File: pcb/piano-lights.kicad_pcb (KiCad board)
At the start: 2 copper layers, 150 x 82 mm, 30 parts, among them J1 FTDI RS232, J2 USB_B_Micro, J3 LED Strip, J4 AVR-ISP-6, J5 MIDI IN, J6 MIDI THRU, SW1 Button, SW2 Reset, U1 ATmega328P-P, U2 H11L1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

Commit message: PCB tweaks
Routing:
- net /DEBUG_TX: track 60.7 -> 61.8 mm
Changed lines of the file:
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@@
     (property "Sheetname" "")
     (attr smd)
-    (fp_text reference "R1" (at 0 -1.65 90) (layer "F.SilkS")
-      (effects (font (size 1 1) (thickness 0.15)))
-    )
-    (fp_text value "2k2" (at 0 1.65 90) (layer "F.Fab")
+    (fp_text reference "R1" (at 2.5 0 180) (layer "F.SilkS")
+      (effects (font (size 1 1) (thickness 0.15)))
+    )
+    (fp_text value "2k2" (at -2.75 0 180) (layer "F.Fab")
       (effects (font (size 1 1) (thickness 0.15)))
     )
@@
     (property "Sheetname" "")
     (attr through_hole)
-    (fp_text reference "C4" (at 1 -3.75 90) (layer "F.SilkS")
-      (effects (font (size 1 1) (thickness 0.15)))
-    )
-    (fp_text value "10u" (at 1 3.75 90) (layer "F.Fab")
+    (fp_text reference "C4" (at -2.75 0 180) (layer "F.SilkS")
+      (effects (font (size 1 1) (thickness 0.15)))
+    )
+    (fp_text value "10u" (at 4.5 0 180) (layer "F.Fab")
       (effects (font (size 1 1) (thickness 0.15)))
     )
@@
     (property "Sheetname" "")
     (attr smd)
-    (fp_text reference "U3" (at 0 -2.9 90) (layer "F.SilkS")
-      (effects (font (size 1 1) (thickness 0.15)))
-    )
-    (fp_text value "74AHC1G125" (at 0 2.9 90) (layer "F.Fab")
+    (fp_text reference "U3" (at 0 -2.9 180) (layer "F.SilkS")
+      (effects (font (size 1 1) (thickness 0.15)))
+    )
+    (fp_text value "74AHC1G125" (at -0.061 6.758 180) (layer "F.Fab")
       (effects (font (size 1 1) (thickness 0.15)))
     )
@@
   (via (at 118.618 97.536) (size 0.762) (drill 0.381) (layers "F.Cu" "B.Cu") (net 4))
   (segment (start 137.17 90.287) (end 137.17 87.112) (width 0.508) (layer "B.Cu") (net 4))
-  (segment (start 176.5 84.044) (end 176.5 78.8) (width 0.508) (layer "B.Cu") (net 4))
+  (segment (start 176.525 88.407) (end 176.525 78.825) (width 0.508) (layer "B.Cu") (net 4))
   (segment (start 119.507 97.536) (end 120.904 98.933) (width 0.508) (layer "B.Cu") (net 4))
   (segment (start 118.618 97.536) (end 119.507 97.536) (width 0.508) (layer "B.Cu") (net 4))
-  (segment (start 176.525 84.069) (end 176.5 84.044) (width 0.508) (layer "B.Cu") (net 4))
   (segment (start 134.63 94.732) (end 134.63 92.827) (width 0.508) (layer "B.Cu") (net 4))
   (segment (start 134.63 92.827) (end 137.17 90.287) (width 0.508) (layer "B.Cu") (net 4))
-  (segment (start 176.525 88.407) (end 176.525 84.069) (width 0.508) (layer "B.Cu") (net 4))
+  (segment (start 176.525 78.825) (end 176.5 78.8) (width 0.508) (layer "B.Cu") (net 4))
   (segment (start 111.52 110.48) (end 110 112) (width 0.254) (layer "F.Cu") (net 5))
   (segment (start 110 112) (end 101.84 112) (width 0.254) (layer "F.Cu") (net 5))
@@
   (segment (start 168.656 108.712) (end 186.944 108.712) (width 0.254) (layer "F.Cu") (net 24))
   (segment (start 153.15 84.8) (end 179.05 84.8) (width 0.254) (layer "F.Cu") (net 25))
-  (segment (start 183.85 84.85) (end 188.3 84.85) (width 0.254) (layer "F.Cu") (net 25))
   (segment (start 179.05 84.8) (end 179.15 84.9) (width 0.254) (layer "F.Cu") (net 25))
   (segment (start 152.41 85.54) (end 153.15 84.8) (width 0.254) (layer "F.Cu") (net 25))
+  (segment (start 189.45 86) (end 189.45 105.55) (width 0.254) (layer "F.Cu") (net 25))
+  (segment (start 183.85 84.85) (end 188.3 84.85) (width 0.254) (layer "F.Cu") (net 25))
   (segment (start 188.3 84.85) (end 189.45 86) (width 0.254) (layer "F.Cu") (net 25))
-  (segment (start 189.45 86) (end 189.45 103.666) (width 0.254) (layer "F.Cu") (net 25))
   (segment (start 152.41 87.112) (end 152.41 85.54) (width 0.254) (layer "F.Cu") (net 25))
-  (segment (start 189.45 103.666) (end 186.944 106.172) (width 0.254) (layer "F.Cu") (net 25))
+  (segment (start 189.45 105.55) (end 188.828 106.172) (width 0.254) (layer "F.Cu") (net 25))
+  (segment (start 188.828 106.172) (end 186.944 106.172) (width 0.254) (layer "F.Cu") (net 25))
   (via (at 183.85 84.85) (size 0.762) (drill 0.381) (layers "F.Cu" "B.Cu") (net 25))
   (via (at 179.15 84.9) (size 0.762) (drill 0.381) (layers "F.Cu" "B.Cu") (net 25))
@@
         (xy 188.1 59)
         (xy 188.08 55)
-        (xy 189.131428 54.999387)
+        (xy 188.53 55)
+        (xy 189.13172 55.499387)
       )
     )

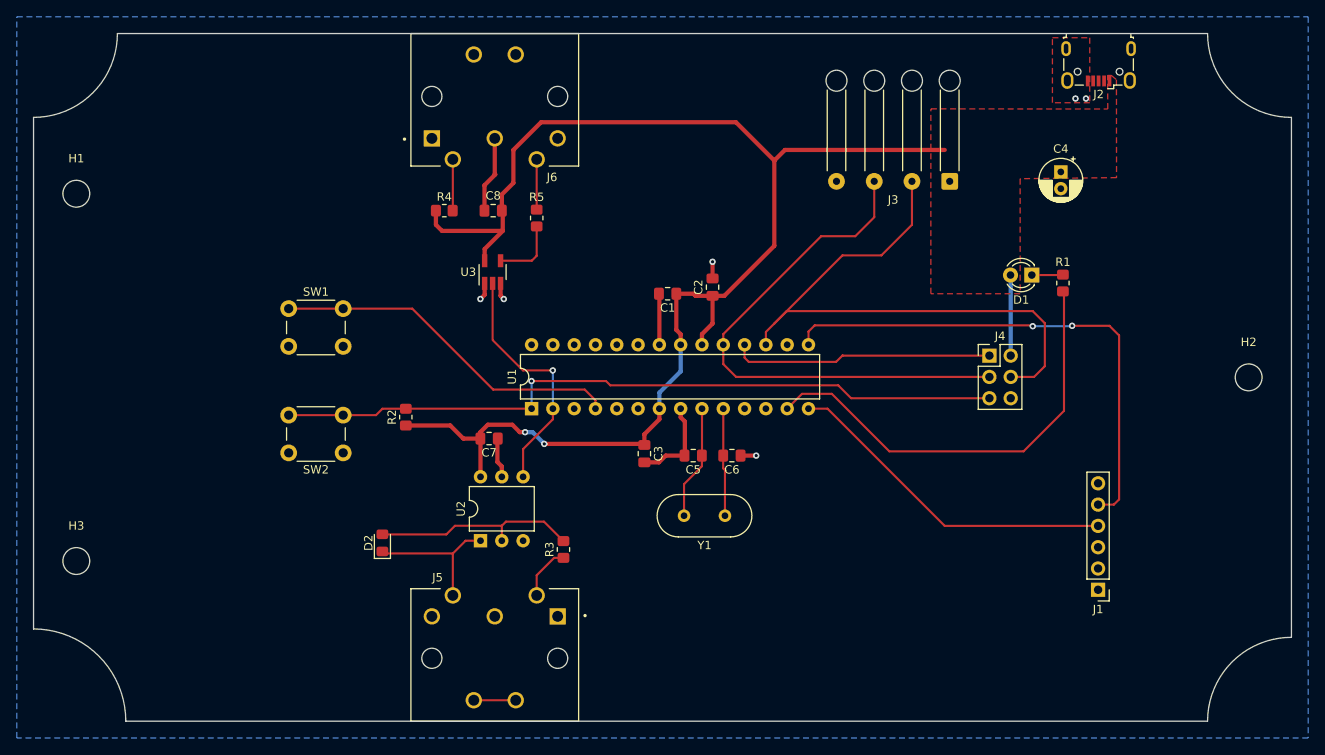
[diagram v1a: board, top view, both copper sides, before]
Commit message: Fix up silk screen. Fix all DRC errors. Tweak position of LED holes.
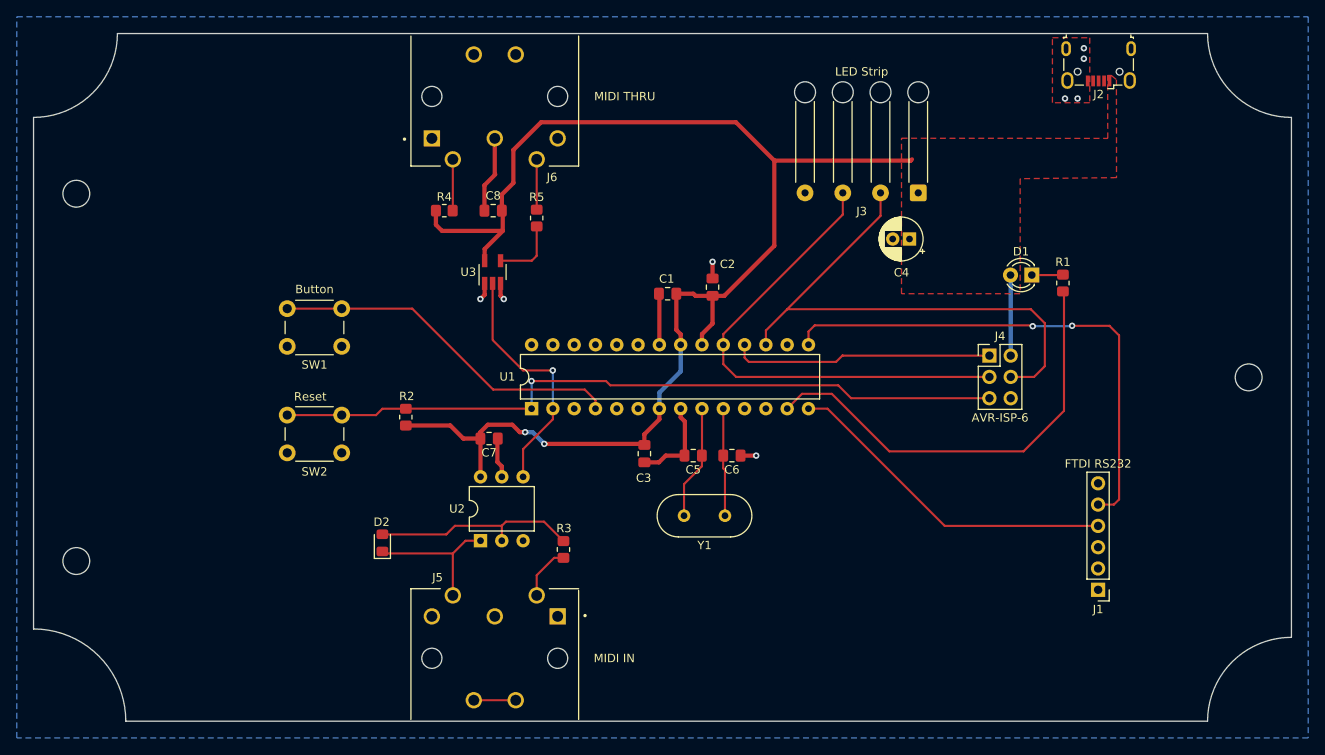
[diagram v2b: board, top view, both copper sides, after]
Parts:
- moved C4 19.7 mm to (164.5, 74.5), turned to 180 degrees
- moved J3 3.99 mm to (165.5, 69.0)
- moved SW2 0.17 mm to (96.8, 100.0)
- moved SW1 0.17 mm to (90.2, 82.8)
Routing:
- net /PICO: track 72.6 -> 64.9 mm
- net /SCK: track 64.0 -> 58.7 mm
- net +5V: track 176.1 -> 171.7 mm
- net GND: track 39.1 -> 39.0 mm, vias 6 -> 8

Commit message: Add a cutout in the side.
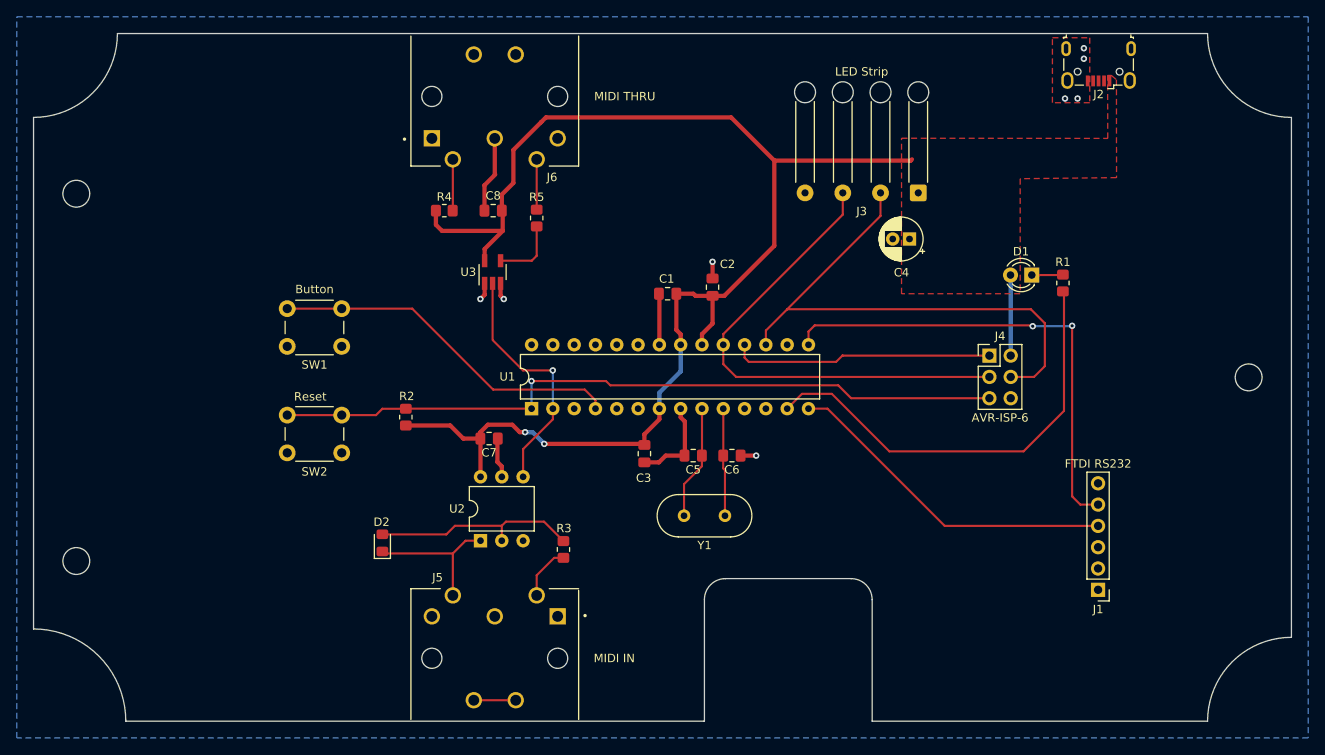
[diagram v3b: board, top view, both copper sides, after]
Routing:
- net /DEBUG_TX: track 61.8 -> 57.2 mm
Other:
- outline, holes or cut-outs redrawn
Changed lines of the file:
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@@
   (gr_arc (start 60 121) (mid 67.778175 124.221825) (end 71 132) (layer "Edge.Cuts") (width 0.1))
   (gr_line (start 200 50) (end 70 50) (layer "Edge.Cuts") (width 0.1))
+  (gr_line (start 140 132) (end 140 117.5) (layer "Edge.Cuts") (width 0.1))
+  (gr_line (start 160 132) (end 200 132) (layer "Edge.Cuts") (width 0.1))
   (gr_line (start 60 60) (end 60 121) (layer "Edge.Cuts") (width 0.1))
   (gr_arc (start 200 132) (mid 202.928932 124.928932) (end 210 122) (layer "Edge.Cuts") (width 0.1))
+  (gr_arc (start 157.5 115) (mid 159.267767 115.732233) (end 160 117.5) (layer "Edge.Cuts") (width 0.1))
+  (gr_line (start 160 117.5) (end 160 132) (layer "Edge.Cuts") (width 0.1))
+  (gr_line (start 142.5 115) (end 157.5 115) (layer "Edge.Cuts") (width 0.1))
   (gr_line (start 210 60) (end 210 122) (layer "Edge.Cuts") (width 0.1))
-  (gr_line (start 71 132) (end 200 132) (layer "Edge.Cuts") (width 0.1))
+  (gr_arc (start 140 117.5) (mid 140.732233 115.732233) (end 142.5 115) (layer "Edge.Cuts") (width 0.1))
+  (gr_line (start 140 132) (end 71 132) (layer "Edge.Cuts") (width 0.1))
   (gr_circle (center 94.85 125) (end 97.85 125) (layer "User.2") (width 0.15) (fill none))
   (gr_arc (start 211 58) (mid 204.636039 55.363961) (end 202 49) (layer "User.2") (width 0.15))
@@
   (segment (start 111.252 98.298) (end 109.696 96.742) (width 0.508) (layer "F.Cu") (net 4))
   (segment (start 132.715 98.933) (end 132.842 99.06) (width 0.508) (layer "F.Cu") (net 4))
+  (segment (start 121.1 60) (end 143.185 60) (width 0.508) (layer "F.Cu") (net 4))
   (segment (start 107.982 71.12) (end 107.982 72.803) (width 0.508) (layer "F.Cu") (net 4))
   (segment (start 113.284 98.298) (end 113.284 97.536) (width 0.508) (layer "F.Cu") (net 4))
@@
   (segment (start 134.63 94.732) (end 134.63 96.002) (width 0.508) (layer "F.Cu") (net 4))
   (segment (start 136.652 81.026) (end 138.684 81.026) (width 0.508) (layer "F.Cu") (net 4))
+  (segment (start 117.221 63.881) (end 120.523 60.579) (width 0.508) (layer "F.Cu") (net 4))
   (segment (start 120.904 98.933) (end 132.715 98.933) (width 0.508) (layer "F.Cu") (net 4))
-  (segment (start 143.764 60.579) (end 148.336 65.151) (width 0.508) (layer "F.Cu") (net 4))
+  (segment (start 115.8455 71.12) (end 115.8455 69.1935) (width 0.508) (layer "F.Cu") (net 4))
   (segment (start 164.599 65.151) (end 164.75 65) (width 0.508) (layer "F.Cu") (net 4))
   (segment (start 113.792 75.692) (end 115.951 73.533) (width 0.508) (layer "F.Cu") (net 4))
@@
   (segment (start 148.336 65.151) (end 164.599 65.151) (width 0.508) (layer "F.Cu") (net 4))
   (segment (start 148.336 75.311) (end 148.336 65.151) (width 0.508) (layer "F.Cu") (net 4))
+  (segment (start 115.8455 69.1935) (end 117.221 67.818) (width 0.508) (layer "F.Cu") (net 4))
   (segment (start 140.97 81.28) (end 142.367 81.28) (width 0.508) (layer "F.Cu") (net 4))
-  (segment (start 117.221 63.881) (end 120.523 60.579) (width 0.508) (layer "F.Cu") (net 4))
   (segment (start 140.97 84.582) (end 140.97 81.28) (width 0.508) (layer "F.Cu") (net 4))
   (segment (start 139.71 85.842) (end 140.97 84.582) (width 0.508) (layer "F.Cu") (net 4))
+  (segment (start 143.185 60) (end 148.336 65.151) (width 0.508) (layer "F.Cu") (net 4))
   (segment (start 134.63 96.002) (end 132.842 97.79) (width 0.508) (layer "F.Cu") (net 4))
   (segment (start 114.173 96.647) (end 117.094 96.647) (width 0.508) (layer "F.Cu") (net 4))
+  (segment (start 120.523 60.579) (end 120.523 60.577) (width 0.508) (layer "F.Cu") (net 4))
   (segment (start 117.094 96.647) (end 117.983 97.536) (width 0.508) (layer "F.Cu") (net 4))
+  (segment (start 108.712 73.533) (end 115.951 73.533) (width 0.508) (layer "F.Cu") (net 4))
+  (segment (start 120.523 60.577) (end 121.1 60) (width 0.508) (layer "F.Cu") (net 4))
+  (segment (start 115.951 71.2255) (end 115.8455 71.12) (width 0.508) (layer "F.Cu") (net 4))
+  (segment (start 137.17 87.112) (end 137.17 85.862) (width 0.508) (layer "F.Cu") (net 4))
   (segment (start 117.221 67.818) (end 117.221 63.881) (width 0.508) (layer "F.Cu") (net 4))
-  (segment (start 120.523 60.579) (end 143.764 60.579) (width 0.508) (layer "F.Cu") (net 4))
-  (segment (start 108.712 73.533) (end 115.951 73.533) (width 0.508) (layer "F.Cu") (net 4))
-  (segment (start 115.951 71.2255) (end 115.8455 71.12) (width 0.508) (layer "F.Cu") (net 4))
-  (segment (start 115.8455 69.1935) (end 117.221 67.818) (width 0.508) (layer "F.Cu") (net 4))
-  (segment (start 137.17 87.112) (end 137.17 85.862) (width 0.508) (layer "F.Cu") (net 4))
-  (segment (start 115.8455 71.12) (end 115.8455 69.1935) (width 0.508) (layer "F.Cu") (net 4))
   (segment (start 136.652 85.344) (end 136.652 81.026) (width 0.508) (layer "F.Cu") (net 4))
   (via (at 120.904 98.933) (size 0.762) (drill 0.381) (layers "F.Cu" "B.Cu") (net 4))
@@
   (segment (start 179.05 84.8) (end 179.15 84.9) (width 0.254) (layer "F.Cu") (net 25))
   (segment (start 152.41 85.54) (end 153.15 84.8) (width 0.254) (layer "F.Cu") (net 25))
-  (segment (start 189.45 86) (end 189.45 105.55) (width 0.254) (layer "F.Cu") (net 25))
-  (segment (start 183.85 84.85) (end 188.3 84.85) (width 0.254) (layer "F.Cu") (net 25))
-  (segment (start 188.3 84.85) (end 189.45 86) (width 0.254) (layer "F.Cu") (net 25))
+  (segment (start 184.828 106.172) (end 183.85 105.194) (width 0.254) (layer "F.Cu") (net 25))
+  (segment (start 184.828 106.172) (end 186.944 106.172) (width 0.254) (layer "F.Cu") (net 25))
+  (segment (start 183.85 84.85) (end 183.85 105.15) (width 0.254) (layer "F.Cu") (net 25))
   (segment (start 152.41 87.112) (end 152.41 85.54) (width 0.254) (layer "F.Cu") (net 25))
-  (segment (start 189.45 105.55) (end 188.828 106.172) (width 0.254) (layer "F.Cu") (net 25))
-  (segment (start 188.828 106.172) (end 186.944 106.172) (width 0.254) (layer "F.Cu") (net 25))
+  (segment (start 183.85 105.194) (end 183.85 105.15) (width 0.254) (layer "F.Cu") (net 25))
   (via (at 183.85 84.85) (size 0.762) (drill 0.381) (layers "F.Cu" "B.Cu") (net 25))
   (via (at 179.15 84.9) (size 0.762) (drill 0.381) (layers "F.Cu" "B.Cu") (net 25))

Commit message: Add some more silk screen info
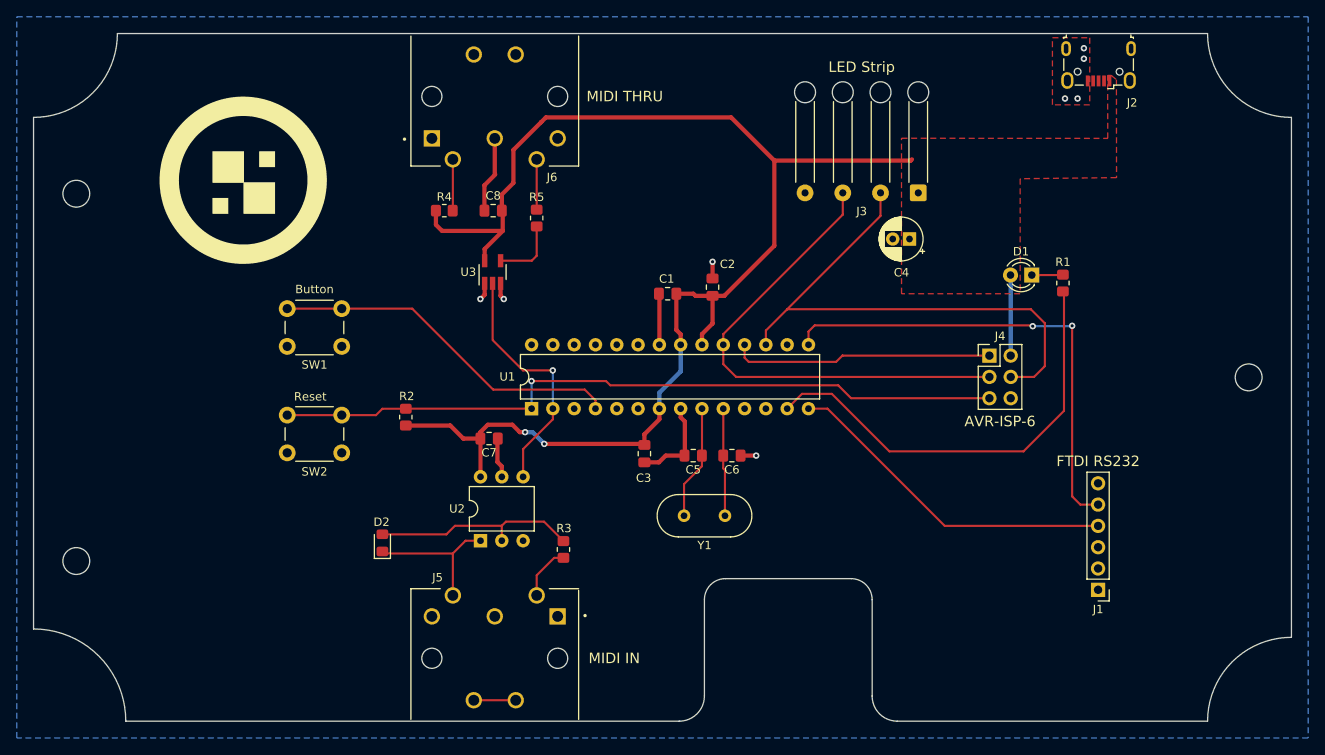
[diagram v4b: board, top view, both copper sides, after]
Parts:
- added G***: LOGO, LOGO, F.Cu at (85.0, 67.5)
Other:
- outline, holes or cut-outs redrawn
- board text added: "Piano Lights v1.0 Dave Dribin"

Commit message: Minor trace tweaks. Move origin to center.
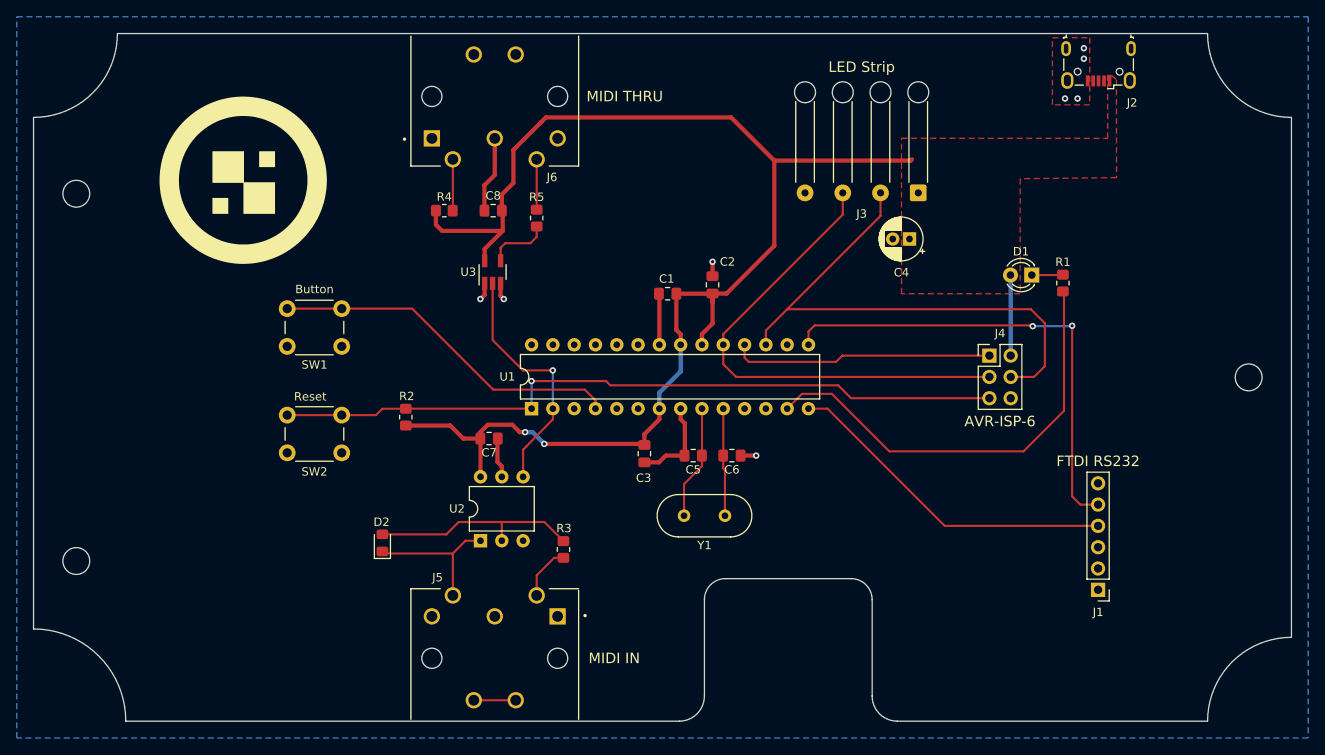
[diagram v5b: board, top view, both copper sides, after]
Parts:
- moved C2 0.28 mm to (141.0, 80.0)
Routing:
- net +5V: track 172.2 -> 173.0 mm

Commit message: Clean up somem more tracks and passive placement
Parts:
- moved U3 1.78 mm to (116.0, 79.8)
- moved R4 1.38 mm to (110.0, 72.0), turned to 90 degrees
- moved C8 0.91 mm to (115.0, 72.0), turned to 90 degrees
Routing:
- net /MIDI_RX: track 29.5 -> 28.4 mm
- net /MTHRU_DATA_R: track 7.63 -> 6.63 mm
- net GND: track 39.0 -> 38.4 mm
